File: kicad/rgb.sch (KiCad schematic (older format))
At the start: 25 parts, among them J1 1935776, J2 Conn_01x05, J3 Conn_01x05, J4 Conn_01x04, J5 Conn_01x02, Q1 DMG9926USD, Q2 DMG9926USD, Q3 DMG9926USD, Q4 DMG9926USD, SW1 SW_Push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

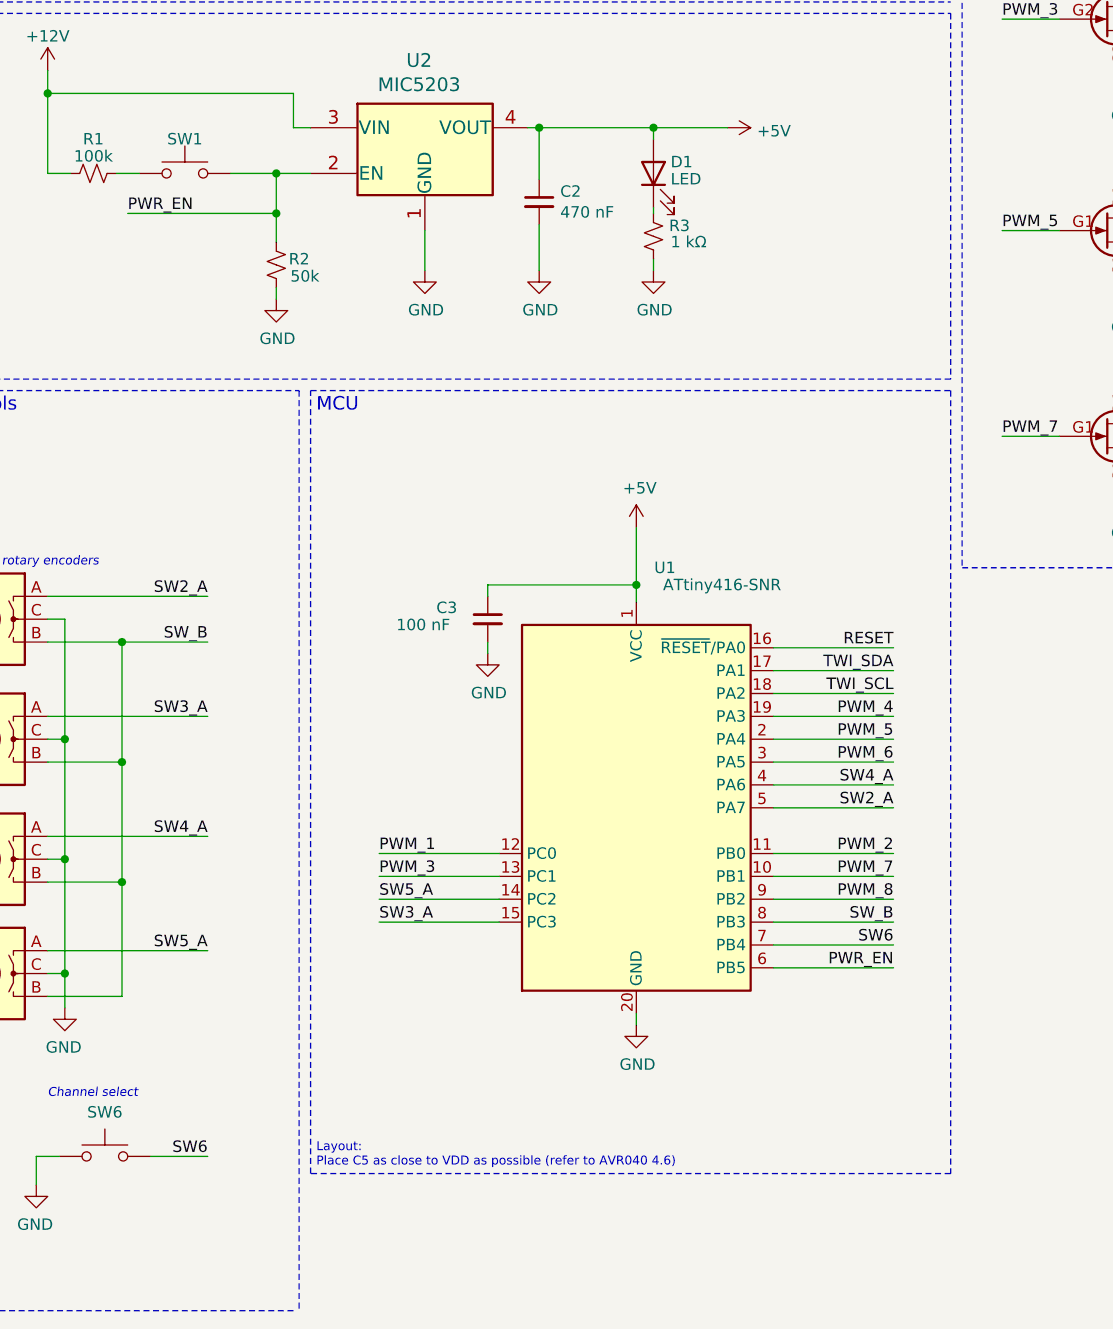
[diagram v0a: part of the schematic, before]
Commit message: New PCB formfactor
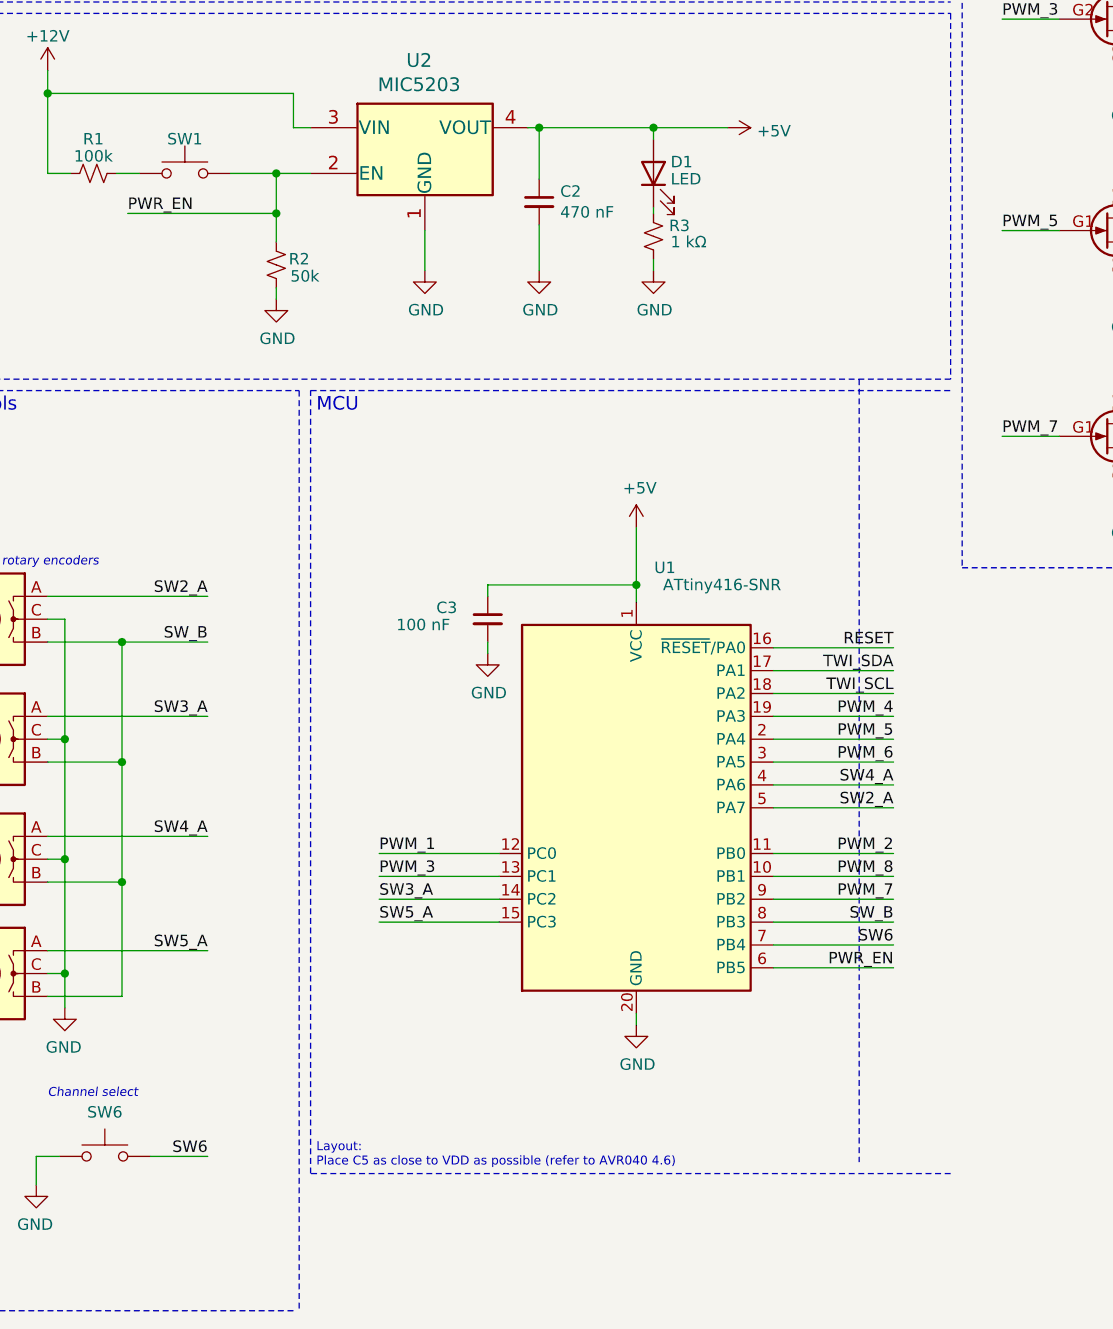
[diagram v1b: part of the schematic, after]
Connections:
- net PWM_7: now also U1.9 (PB2); no longer U1.10 (PB1)
- net PWM_8: now also U1.10 (PB1); no longer U1.9 (PB2)
- net PWR_EN: now also SW1.1; no longer SW1.2
- net SW3_A: now also U1.14 (PC2); no longer U1.15 (PC3)
- net SW5_A: now also U1.15 (PC3); no longer U1.14 (PC2)
- net at R1.1: now also SW1.2; no longer SW1.1
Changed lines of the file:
@@
 F 3 "~" H 2000 3050 50  0001 C CNN
 	1    2000 2850
-	1    0    0    -1
+	-1   0    0    -1
 $EndComp
 $Comp
@@
 	5350 7225 2550 7225
 Wire Notes Line
-	5350 3800 5350 7225
+	4950 3750 4950 7175
 Wire Wire Line
 	3975 4650 3975 4725
@@
 Wire Wire Line
 	4575 5025 5100 5025
-Text Label 2850 6025 0    50   ~ 0
+Text Label 2850 6125 0    50   ~ 0
 SW5_A
 Wire Wire Line
@@
 SW2_A
 Wire Wire Line
+	3375 6125 2850 6125
+Text Label 2850 6025 0    50   ~ 0
+SW3_A
+Wire Wire Line
 	3375 6025 2850 6025
-Text Label 2850 6125 0    50   ~ 0
-SW3_A
-Wire Wire Line
-	3375 6125 2850 6125
 Text Label 5100 6225 2    50   ~ 0
 SW6
@@
 Wire Wire Line
 	4575 5925 5100 5925
+Text Label 5100 6025 2    50   ~ 0
+PWM_7
+Wire Wire Line
+	3375 5825 2850 5825
 Text Label 5100 5925 2    50   ~ 0
-PWM_7
-Wire Wire Line
-	3375 5825 2850 5825
-Text Label 5100 6025 2    50   ~ 0
 PWM_8
 Wire Wire Line

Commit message: minor layout changes
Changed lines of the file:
@@
 	5350 7225 2550 7225
 Wire Notes Line
-	4950 3750 4950 7175
+	5350 3800 5350 7225
 Wire Wire Line
 	3975 4650 3975 4725

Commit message: dcdc layout
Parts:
- added TP1, TP2, TP3, TP4, TP5, TP6, TP7, TP8: TestPoint, TestPoint:TestPoint_Pad_D2.0mm, symbol Connector:TestPoint
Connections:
- wire segments 135 -> 143
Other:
- note added: "Test Points\n"
- moved on the sheet: C2, D1, R1, R2, R3, SW1, U2

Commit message: datasheets and model numbers
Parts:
- removed TP1, TP2, TP3, TP4, TP5, TP6, TP7, TP8: TestPoint, TestPoint:TestPoint_Pad_D2.0mm, symbol Connector:TestPoint
- D1: value LED -> 732-4987-2-ND
- J2, J3: value Conn_01x05 -> 102-6164-ND
- SW1, SW6: value SW_Push -> 450-1642-ND
- SW2, SW3, SW4, SW5: value Rotary_Encoder -> PEC12R-4220F-N0024
- U2: value MIC5203 -> 576-1256-2-ND
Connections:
- wire segments 143 -> 135
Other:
- note removed: "Test Points\n"
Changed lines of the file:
@@
 P 4125 2850
 F 0 "D1" V 4175 2775 50  0000 R CNN
-F 1 "LED" V 4100 2775 50  0000 R CNN
+F 1 "732-4987-2-ND" V 4100 2775 50  0000 R CNN
 F 2 "LED_SMD:LED_0805_2012Metric_Pad1.15x1.40mm_HandSolder" H 4125 2850 50  0001 C CNN
-F 3 "~" H 4125 2850 50  0001 C CNN
+F 3 "https://www.we-online.de/katalog/datasheet/150080YS75000.pdf" H 4125 2850 50  0001 C CNN
 	1    4125 2850
 	0    -1   -1   0
@@
 P 1650 7150
 F 0 "SW6" H 1650 7343 50  0000 C CNN
-F 1 "SW_Push" H 1650 7344 50  0001 C CNN
+F 1 "450-1642-ND" H 1650 7344 50  0001 C CNN
 F 2 "Button_Switch_THT:SW_PUSH_6mm_H13mm" H 1650 7350 50  0001 C CNN
-F 3 "~" H 1650 7350 50  0001 C CNN
+F 3 "https://www.te.com/commerce/DocumentDelivery/DDEController?Action=srchrtrv&DocNm=1825910&DocType=Customer+Drawing&DocLang=English" H 1650 7350 50  0001 C CNN
 	1    1650 7150
 	-1   0    0    -1
@@
 P 1100 6350
 F 0 "SW5" H 1330 6350 50  0000 L CNN
-F 1 "Rotary_Encoder" H 1330 6305 50  0001 L CNN
+F 1 "PEC12R-4220F-N0024" H 1330 6305 50  0001 L CNN
 F 2 "rgb_footprints:rotary encoder" H 950 6510 50  0001 C CNN
-F 3 "~" H 1100 6610 50  0001 C CNN
+F 3 "https://www.bourns.com/docs/Product-Datasheets/PEC12R.pdf" H 1100 6610 50  0001 C CNN
 	1    1100 6350
 	-1   0    0    -1
@@
 P 1100 5850
 F 0 "SW4" H 1330 5850 50  0000 L CNN
-F 1 "Rotary_Encoder" H 1330 5805 50  0001 L CNN
+F 1 "PEC12R-4220F-N0024" H 1330 5805 50  0001 L CNN
 F 2 "rgb_footprints:rotary encoder" H 950 6010 50  0001 C CNN
-F 3 "~" H 1100 6110 50  0001 C CNN
+F 3 "https://www.bourns.com/docs/Product-Datasheets/PEC12R.pdf" H 1100 6110 50  0001 C CNN
 	1    1100 5850
 	-1   0    0    -1
@@
 P 1100 4800
 F 0 "SW2" H 1330 4800 50  0000 L CNN
-F 1 "Rotary_Encoder" H 1330 4755 50  0001 L CNN
+F 1 "PEC12R-4220F-N0024" H 1330 4755 50  0001 L CNN
 F 2 "rgb_footprints:rotary encoder" H 950 4960 50  0001 C CNN
-F 3 "~" H 1100 5060 50  0001 C CNN
+F 3 "https://www.bourns.com/docs/Product-Datasheets/PEC12R.pdf" H 1100 5060 50  0001 C CNN
 	1    1100 4800
 	-1   0    0    -1
@@
 P 1100 5325
 F 0 "SW3" H 1330 5325 50  0000 L CNN
-F 1 "Rotary_Encoder" H 1330 5280 50  0001 L CNN
+F 1 "PEC12R-4220F-N0024" H 1330 5280 50  0001 L CNN
 F 2 "rgb_footprints:rotary encoder" H 950 5485 50  0001 C CNN
-F 3 "~" H 1100 5585 50  0001 C CNN
+F 3 "https://www.bourns.com/docs/Product-Datasheets/PEC12R.pdf" H 1100 5585 50  0001 C CNN
 	1    1100 5325
 	-1   0    0    -1
@@
 P 2075 2850
 F 0 "SW1" H 2075 3000 50  0000 C CNN
-F 1 "SW_Push" H 2075 3044 50  0001 C CNN
+F 1 "450-1642-ND" H 2075 3044 50  0001 C CNN
 F 2 "Button_Switch_THT:SW_PUSH_6mm_H13mm" H 2075 3050 50  0001 C CNN
-F 3 "~" H 2075 3050 50  0001 C CNN
+F 3 "https://www.te.com/commerce/DocumentDelivery/DDEController?Action=srchrtrv&DocNm=1825910&DocType=Customer+Drawing&DocLang=English" H 2075 3050 50  0001 C CNN
 	1    2075 2850
 	-1   0    0    -1
@@
 P 3125 2950
 F 0 "U2" H 3100 3544 60  0000 C CNN
-F 1 "MIC5203" H 3100 3438 60  0000 C CNN
+F 1 "576-1256-2-ND" H 3100 3438 60  0000 C CNN
 F 2 "digikey-footprints:SOT-143-4" H 4225 3190 60  0001 C CNN
 F 3 "" H 3125 2950 60  0000 C CNN
@@
 P 9000 1325
 F 0 "J2" H 8950 1625 50  0000 L CNN
-F 1 "Conn_01x05" H 9080 1276 50  0001 L CNN
+F 1 "102-6164-ND" H 9080 1276 50  0001 L CNN
 F 2 "rgb_footprints:CUI_TB003-500-P05BE" H 9000 1325 50  0001 C CNN
 F 3 "~" H 9000 1325 50  0001 C CNN
@@
 P 9000 2250
 F 0 "J3" H 8950 2550 50  0000 L CNN
-F 1 "Conn_01x05" H 8918 1916 50  0001 C CNN
+F 1 "102-6164-ND" H 8918 1916 50  0001 C CNN
 F 2 "rgb_footprints:CUI_TB003-500-P05BE" H 9000 2250 50  0001 C CNN
 F 3 "~" H 9000 2250 50  0001 C CNN
@@
 Text Label 5100 5825 2    50   ~ 0
 PWM_2
-$Comp
-L Connector:TestPoint TP1
-U 1 1 5FFF62D8
-P 6925 5150
-F 0 "TP1" V 6925 5338 50  0000 L CNN
-F 1 "TestPoint" V 6970 5338 50  0001 L CNN
-F 2 "TestPoint:TestPoint_Pad_D2.0mm" H 7125 5150 50  0001 C CNN
-F 3 "~" H 7125 5150 50  0001 C CNN
-	1    6925 5150
-	0    1    1    0
-$EndComp
-Text Label 6300 5150 0    50   ~ 0
-PWM_1
-Wire Wire Line
-	6300 5150 6925 5150
-$Comp
-L Connector:TestPoint TP2
-U 1 1 6005165A
-P 6925 5275
-F 0 "TP2" V 6925 5463 50  0000 L CNN
-F 1 "TestPoint" V 6970 5463 50  0001 L CNN
-F 2 "TestPoint:TestPoint_Pad_D2.0mm" H 7125 5275 50  0001 C CNN
-F 3 "~" H 7125 5275 50  0001 C CNN
-	1    6925 5275
-	0    1    1    0
-$EndComp
-Text Label 6300 5275 0    50   ~ 0
-PWM_2
-Wire Wire Line
-	6300 5275 6925 5275
-$Comp
-L Connector:TestPoint TP3
-U 1 1 60056081
-P 6925 5400
-F 0 "TP3" V 6925 5588 50  0000 L CNN
-F 1 "TestPoint" V 6970 5588 50  0001 L CNN
-F 2 "TestPoint:TestPoint_Pad_D2.0mm" H 7125 5400 50  0001 C CNN
-F 3 "~" H 7125 5400 50  0001 C CNN
-	1    6925 5400
-	0    1    1    0
-$EndComp
-Text Label 6300 5400 0    50   ~ 0
-PWM_3
-Wire Wire Line
-	6300 5400 6925 5400
-$Comp
-L Connector:TestPoint TP4
-U 1 1 6005C178
-P 6925 5525
-F 0 "TP4" V 6925 5713 50  0000 L CNN
-F 1 "TestPoint" V 6970 5713 50  0001 L CNN
-F 2 "TestPoint:TestPoint_Pad_D2.0mm" H 7125 5525 50  0001 C CNN
-F 3 "~" H 7125 5525 50  0001 C CNN
-	1    6925 5525
-	0    1    1    0
-$EndComp
-Text Label 6300 5525 0    50   ~ 0
-PWM_4
-Wire Wire Line
-	6300 5525 6925 5525
-$Comp
-L Connector:TestPoint TP5
-U 1 1 6005C180
-P 6925 5650
-F 0 "TP5" V 6925 5838 50  0000 L CNN
-F 1 "TestPoint" V 6970 5838 50  0001 L CNN
-F 2 "TestPoint:TestPoint_Pad_D2.0mm" H 7125 5650 50  0001 C CNN
-F 3 "~" H 7125 5650 50  0001 C CNN
-	1    6925 5650
-	0    1    1    0
-$EndComp
-Text Label 6300 5650 0    50   ~ 0
-PWM_5
-Wire Wire Line
-	6300 5650 6925 5650
-$Comp
-L Connector:TestPoint TP6
-U 1 1 6005C188
-P 6925 5775
-F 0 "TP6" V 6925 5963 50  0000 L CNN
-F 1 "TestPoint" V 6970 5963 50  0001 L CNN
-F 2 "TestPoint:TestPoint_Pad_D2.0mm" H 7125 5775 50  0001 C CNN
-F 3 "~" H 7125 5775 50  0001 C CNN
-	1    6925 5775
-	0    1    1    0
-$EndComp
-Text Label 6300 5775 0    50   ~ 0
-PWM_6
-Wire Wire Line
-	6300 5775 6925 5775
-$Comp
-L Connector:TestPoint TP7
-U 1 1 60061EB4
-P 6925 5900
-F 0 "TP7" V 6925 6088 50  0000 L CNN
-F 1 "TestPoint" V 6970 6088 50  0001 L CNN
-F 2 "TestPoint:TestPoint_Pad_D2.0mm" H 7125 5900 50  0001 C CNN
-F 3 "~" H 7125 5900 50  0001 C CNN
-	1    6925 5900
-	0    1    1    0
-$EndComp
-Text Label 6300 5900 0    50   ~ 0
-PWM_7
-Wire Wire Line
-	6300 5900 6925 5900
-$Comp
-L Connector:TestPoint TP8
-U 1 1 60061EBC
-P 6925 6025
-F 0 "TP8" V 6925 6213 50  0000 L CNN
-F 1 "TestPoint" V 6970 6213 50  0001 L CNN
-F 2 "TestPoint:TestPoint_Pad_D2.0mm" H 7125 6025 50  0001 C CNN
-F 3 "~" H 7125 6025 50  0001 C CNN
-	1    6925 6025
-	0    1    1    0
-$EndComp
-Text Label 6300 6025 0    50   ~ 0
-PWM_8
-Wire Wire Line
-	6300 6025 6925 6025
-Wire Notes Line
-	5400 4625 5400 6700
-Wire Notes Line
-	5400 6700 8125 6700
-Wire Notes Line
-	8125 6700 8125 4625
-Wire Notes Line
-	8125 4625 5400 4625
-Text Notes 5425 4750 0    59   ~ 0
-Test Points\n
 $EndSCHEMATC
